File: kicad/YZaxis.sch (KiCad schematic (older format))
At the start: 34 parts, among them CON16 YZ, CON17 Stepstick_Left_Connector, CON18 Stepstick_Right_Connector, CON19 Stepstick_Left_Connector, CON20 Stepstick_Right_Connector, Q5 IRLR2905ZPBF, Q6 FDC6401N, U1 CD4504BPW

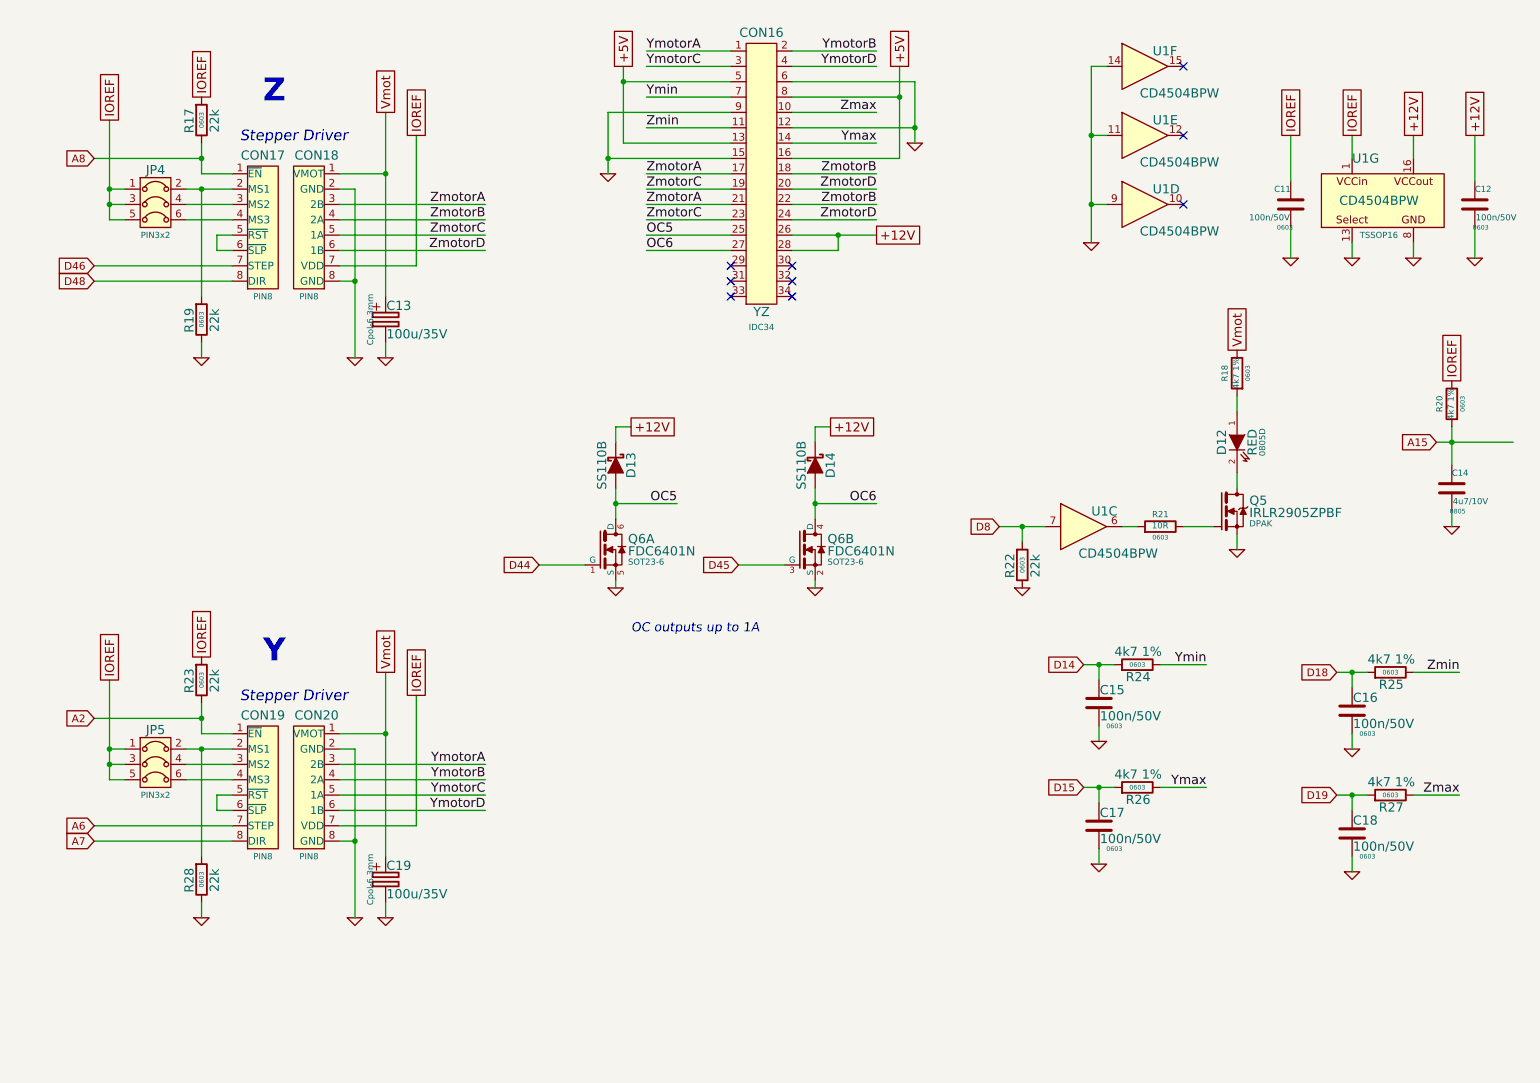
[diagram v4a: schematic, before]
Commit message: Add footprint informations
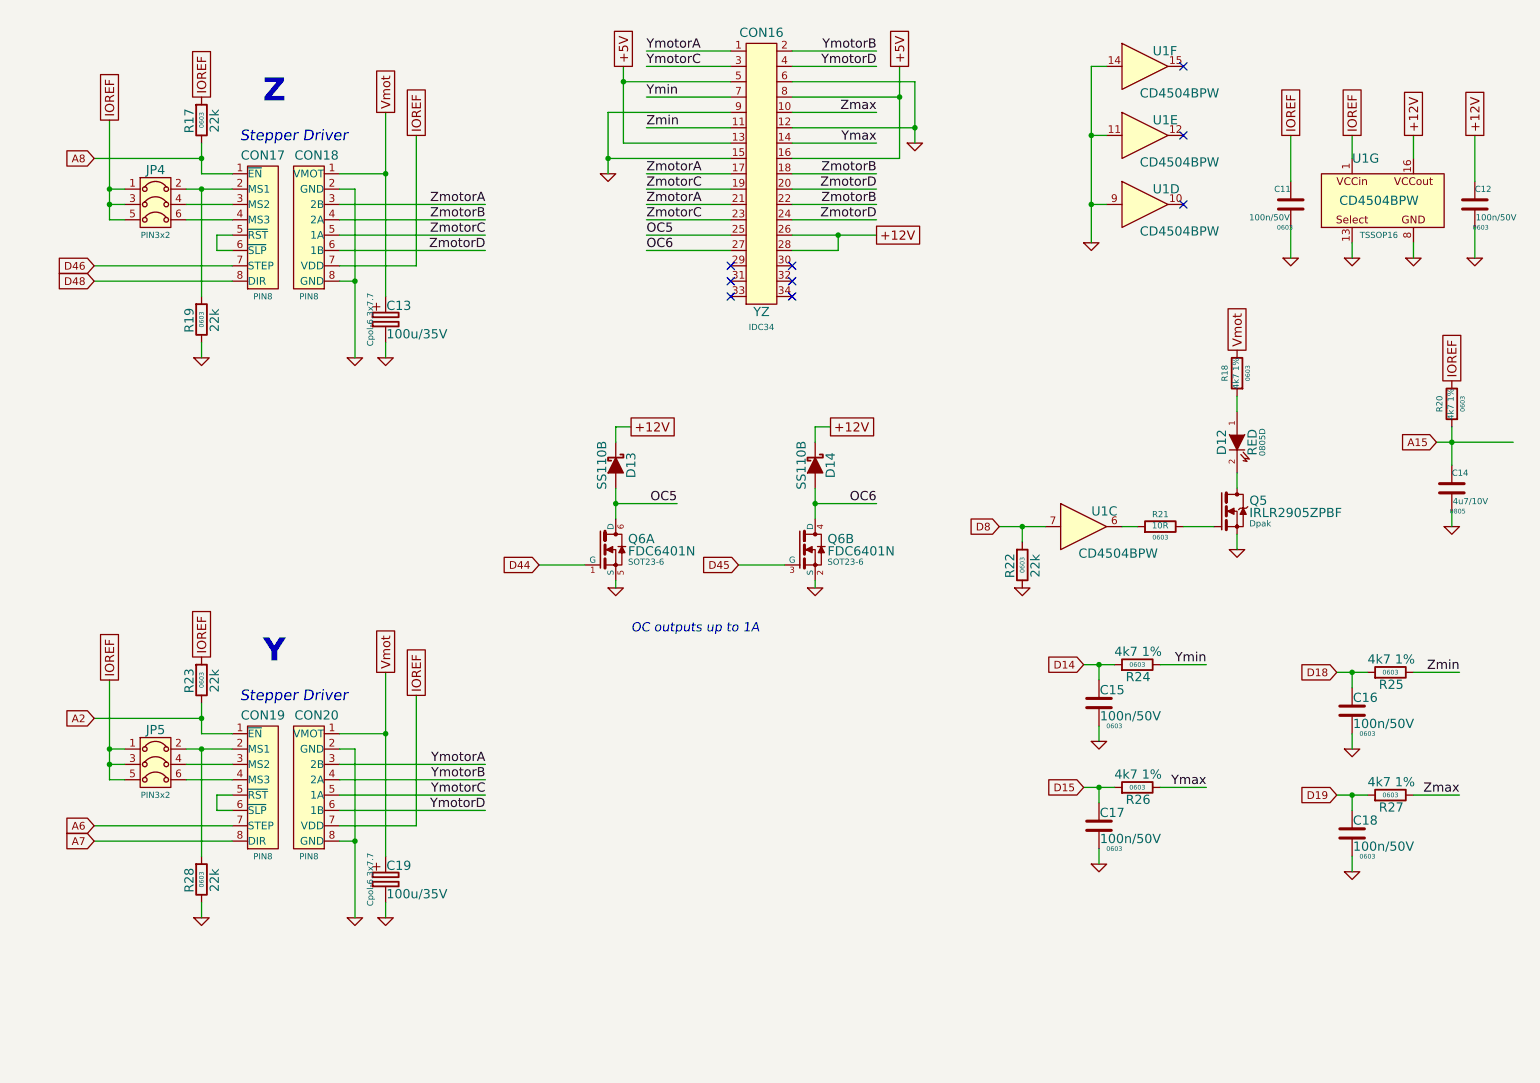
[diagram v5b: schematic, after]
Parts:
- C13, C19: footprint Cpol-6.3mm -> Cpol-6.3x7.7
- Q5: footprint DPAK -> Dpak
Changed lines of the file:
@@
 A7
 $Comp
-L GND #PWR38
+L GND #PWR027
 U 1 1 534EC7A3
 P 8750 4150
-F 0 "#PWR38" H 8750 4150 30  0001 C CNN
+F 0 "#PWR027" H 8750 4150 30  0001 C CNN
 F 1 "GND" H 8750 4080 30  0001 C CNN
 F 2 "~" H 8750 4150 60  0000 C CNN
@@
 $EndComp
 $Comp
-L GND #PWR37
+L GND #PWR028
 U 1 1 534ECB96
 P 10150 4000
-F 0 "#PWR37" H 10150 4000 30  0001 C CNN
+F 0 "#PWR028" H 10150 4000 30  0001 C CNN
 F 1 "GND" H 10150 3930 30  0001 C CNN
 F 2 "~" H 10150 4000 60  0000 C CNN
@@
 Connection ~ 10150 3450
 $Comp
-L GND #PWR32
+L GND #PWR029
 U 1 1 534ED3BB
 P 9900 2250
-F 0 "#PWR32" H 9900 2250 30  0001 C CNN
+F 0 "#PWR029" H 9900 2250 30  0001 C CNN
 F 1 "GND" H 9900 2180 30  0001 C CNN
 F 2 "~" H 9900 2250 60  0000 C CNN
@@
 $EndComp
 $Comp
-L GND #PWR33
+L GND #PWR030
 U 1 1 534ED3D4
 P 10300 2250
-F 0 "#PWR33" H 10300 2250 30  0001 C CNN
+F 0 "#PWR030" H 10300 2250 30  0001 C CNN
 F 1 "GND" H 10300 2180 30  0001 C CNN
 F 2 "~" H 10300 2250 60  0000 C CNN
@@
 $EndComp
 $Comp
-L GND #PWR30
+L GND #PWR031
 U 1 1 534ED3DA
 P 9100 2250
-F 0 "#PWR30" H 9100 2250 30  0001 C CNN
+F 0 "#PWR031" H 9100 2250 30  0001 C CNN
 F 1 "GND" H 9100 2180 30  0001 C CNN
 F 2 "~" H 9100 2250 60  0000 C CNN
@@
 	7200 4000 7500 4000
 $Comp
-L GND #PWR41
+L GND #PWR032
 U 1 1 536FED2A
 P 7350 4400
-F 0 "#PWR41" H 7350 4400 30  0001 C CNN
+F 0 "#PWR032" H 7350 4400 30  0001 C CNN
 F 1 "GND" H 7350 4330 30  0001 C CNN
 F 2 "~" H 7350 4400 60  0000 C CNN
@@
 F 0 "Q5" H 8830 4070 60  0000 L CNN
 F 1 "IRLR2905ZPBF" H 8830 3990 60  0000 L CNN
-F 2 "DPAK" H 8830 3920 40  0000 L CNN
+F 2 "Dpak" H 8830 3920 40  0000 L CNN
 F 3 "" H 8650 3950 60  0000 C CNN
 	1    8650 3950
@@
 	7850 5300 7850 5400
 $Comp
-L GND #PWR42
+L GND #PWR033
 U 1 1 537E6A4E
 P 7850 5400
-F 0 "#PWR42" H 7850 5400 30  0001 C CNN
+F 0 "#PWR033" H 7850 5400 30  0001 C CNN
 F 1 "GND" H 7850 5330 30  0001 C CNN
 F 2 "~" H 7850 5400 60  0000 C CNN
@@
 	7850 6100 7850 6200
 $Comp
-L GND #PWR44
+L GND #PWR034
 U 1 1 537E6A65
 P 7850 6200
-F 0 "#PWR44" H 7850 6200 30  0001 C CNN
+F 0 "#PWR034" H 7850 6200 30  0001 C CNN
 F 1 "GND" H 7850 6130 30  0001 C CNN
 F 2 "~" H 7850 6200 60  0000 C CNN
@@
 	9500 5350 9500 5450
 $Comp
-L GND #PWR43
+L GND #PWR035
 U 1 1 537E6A80
 P 9500 5450
-F 0 "#PWR43" H 9500 5450 30  0001 C CNN
+F 0 "#PWR035" H 9500 5450 30  0001 C CNN
 F 1 "GND" H 9500 5380 30  0001 C CNN
 F 2 "~" H 9500 5450 60  0000 C CNN
@@
 	9500 6150 9500 6250
 $Comp
-L GND #PWR45
+L GND #PWR036
 U 1 1 537E6A97
 P 9500 6250
-F 0 "#PWR45" H 9500 6250 30  0001 C CNN
+F 0 "#PWR036" H 9500 6250 30  0001 C CNN
 F 1 "GND" H 9500 6180 30  0001 C CNN
 F 2 "~" H 9500 6250 60  0000 C CNN
@@
 	6400 1800 5850 1800
 $Comp
-L GND #PWR27
+L GND #PWR037
 U 1 1 537E6E27
 P 6650 1500
-F 0 "#PWR27" H 6650 1500 30  0001 C CNN
+F 0 "#PWR037" H 6650 1500 30  0001 C CNN
 F 1 "GND" H 6650 1430 30  0001 C CNN
 F 2 "~" H 6650 1500 60  0000 C CNN
@@
 	4750 1000 4750 1500
 $Comp
-L GND #PWR28
+L GND #PWR038
 U 1 1 537E72EF
 P 4650 1700
-F 0 "#PWR28" H 4650 1700 30  0001 C CNN
+F 0 "#PWR038" H 4650 1700 30  0001 C CNN
 F 1 "GND" H 4650 1630 30  0001 C CNN
 F 2 "~" H 4650 1700 60  0000 C CNN
@@
 Connection ~ 7800 1450
 $Comp
-L GND #PWR29
+L GND #PWR039
 U 1 1 538D7812
 P 7800 2150
-F 0 "#PWR29" H 7800 2150 30  0001 C CNN
+F 0 "#PWR039" H 7800 2150 30  0001 C CNN
 F 1 "GND" H 7800 2080 30  0001 C CNN
 F 2 "~" H 7800 2150 60  0000 C CNN
@@
 $EndComp
 $Comp
-L GND #PWR31
+L GND #PWR040
 U 1 1 538D791A
 P 9500 2250
-F 0 "#PWR31" H 9500 2250 30  0001 C CNN
+F 0 "#PWR040" H 9500 2250 30  0001 C CNN
 F 1 "GND" H 9500 2180 30  0001 C CNN
 F 2 "~" H 9500 2250 60  0000 C CNN
@@
 $EndComp
 $Comp
-L GND #PWR39
+L GND #PWR041
 U 1 1 53924614
 P 4700 4400
-F 0 "#PWR39" H 4700 4400 30  0001 C CNN
+F 0 "#PWR041" H 4700 4400 30  0001 C CNN
 F 1 "GND" H 4700 4330 30  0001 C CNN
 F 2 "~" H 4700 4400 60  0000 C CNN
@@
 	4700 4400 4700 4350
 $Comp
-L GND #PWR40
+L GND #PWR042
 U 1 1 5392461B
 P 6000 4400
-F 0 "#PWR40" H 6000 4400 30  0001 C CNN
+F 0 "#PWR042" H 6000 4400 30  0001 C CNN
 F 1 "GND" H 6000 4330 30  0001 C CNN
 F 2 "~" H 6000 4400 60  0000 C CNN
@@
 	2000 1700 2200 1700
 Wire Wire Line
-	2000 1800 2200 1800
-Wire Wire Line
-	1900 1800 2000 1800
+	1900 1800 2200 1800
 Wire Wire Line
 	2200 1900 1900 1900
@@
 	2900 2400 3000 2400
 Wire Wire Line
-	3000 2400 3000 2900
-Wire Wire Line
-	3000 1800 3000 2400
+	3000 1800 3000 2900
 Wire Wire Line
 	3000 1800 2900 1800
@@
 	2900 1700 3200 1700
 Wire Wire Line
-	3200 1700 3200 2500
-Wire Wire Line
-	3200 1300 3200 1700
+	3200 1300 3200 2500
 Wire Wire Line
 	2900 2300 3400 2300
@@
 	3400 2300 3400 1450
 Wire Wire Line
-	2000 1600 2000 1700
-Wire Wire Line
-	2000 1500 2000 1600
+	2000 1500 2000 1700
 Wire Wire Line
 	1300 1600 2000 1600
@@
 	1400 2000 1500 2000
 Wire Wire Line
-	1400 1900 1400 2000
-Wire Wire Line
-	1400 1800 1400 1900
-Wire Wire Line
-	1400 1350 1400 1800
+	1400 1350 1400 2000
 Wire Wire Line
 	1500 1800 1400 1800
@@
 F 0 "C13" H 3205 2740 60  0000 L CNN
 F 1 "100u/35V" H 3205 2555 60  0000 L CNN
-F 2 "Cpol-6.3mm" V 3100 2650 40  0000 C CNN
+F 2 "Cpol-6.3x7.7" V 3100 2650 40  0000 C CNN
 F 3 "" H 3200 2640 60  0000 C CNN
 	1    3200 2650
@@
 $EndComp
 $Comp
-L GND #PWR36
+L GND #PWR043
 U 1 1 539A1B02
 P 3200 2900
-F 0 "#PWR36" H 3200 2900 30  0001 C CNN
+F 0 "#PWR043" H 3200 2900 30  0001 C CNN
 F 1 "GND" H 3200 2830 30  0001 C CNN
 F 2 "~" H 3200 2900 60  0000 C CNN
@@
 Z
 $Comp
-L GND #PWR34
+L GND #PWR044
 U 1 1 539A1B17
 P 2000 2900
-F 0 "#PWR34" H 2000 2900 30  0001 C CNN
+F 0 "#PWR044" H 2000 2900 30  0001 C CNN
 F 1 "GND" H 2000 2830 30  0001 C CNN
 F 2 "~" H 2000 2900 60  0000 C CNN
@@
 $EndComp
 $Comp
-L GND #PWR35
+L GND #PWR045
 U 1 1 539A1B1D
 P 3000 2900
-F 0 "#PWR35" H 3000 2900 30  0001 C CNN
+F 0 "#PWR045" H 3000 2900 30  0001 C CNN
 F 1 "GND" H 3000 2830 30  0001 C CNN
 F 2 "~" H 3000 2900 60  0000 C CNN
@@
 	2000 5350 2200 5350
 Wire Wire Line
-	2000 5450 2200 5450
-Wire Wire Line
-	1900 5450 2000 5450
+	1900 5450 2200 5450
 Wire Wire Line
 	2200 5550 1900 5550
@@
 	2900 6050 3000 6050
 Wire Wire Line
-	3000 6050 3000 6550
-Wire Wire Line
-	3000 5450 3000 6050
+	3000 5450 3000 6550
 Wire Wire Line
 	3000 5450 2900 5450
@@
 	2900 5350 3200 5350
 Wire Wire Line
-	3200 5350 3200 6150
-Wire Wire Line
-	3200 4950 3200 5350
+	3200 4950 3200 6150
 Wire Wire Line
 	2900 5950 3400 5950
@@
 	3400 5950 3400 5100
 Wire Wire Line
-	2000 5250 2000 5350
-Wire Wire Line
-	2000 5150 2000 5250
+	2000 5150 2000 5350
 Wire Wire Line
 	1300 5250 2000 5250
@@
 	1400 5650 1500 5650
 Wire Wire Line
-	1400 5550 1400 5650
-Wire Wire Line
-	1400 5450 1400 5550
-Wire Wire Line
-	1400 5000 1400 5450
+	1400 5000 1400 5650
 Wire Wire Line
 	1500 5450 1400 5450
@@
 F 0 "C19" H 3205 6390 60  0000 L CNN
 F 1 "100u/35V" H 3205 6205 60  0000 L CNN
-F 2 "Cpol-6.3mm" V 3100 6300 40  0000 C CNN
+F 2 "Cpol-6.3x7.7" V 3100 6300 40  0000 C CNN
 F 3 "" H 3200 6290 60  0000 C CNN
 	1    3200 6300
@@
 $EndComp
 $Comp
-L GND #PWR48
+L GND #PWR046
 U 1 1 539A1C4E
 P 3200 6550
-F 0 "#PWR48" H 3200 6550 30  0001 C CNN
+F 0 "#PWR046" H 3200 6550 30  0001 C CNN
 F 1 "GND" H 3200 6480 30  0001 C CNN
 F 2 "~" H 3200 6550 60  0000 C CNN
@@
 Y
 $Comp
-L GND #PWR46
+L GND #PWR047
 U 1 1 539A1C63
 P 2000 6550
-F 0 "#PWR46" H 2000 6550 30  0001 C CNN
+F 0 "#PWR047" H 2000 6550 30  0001 C CNN
 F 1 "GND" H 2000 6480 30  0001 C CNN
 F 2 "~" H 2000 6550 60  0000 C CNN
@@
 $EndComp
 $Comp
-L GND #PWR47
+L GND #PWR048
 U 1 1 539A1C69
 P 3000 6550
-F 0 "#PWR47" H 3000 6550 30  0001 C CNN
+F 0 "#PWR048" H 3000 6550 30  0001 C CNN
 F 1 "GND" H 3000 6480 30  0001 C CNN
 F 2 "~" H 3000 6550 60  0000 C CNN

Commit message: Place components
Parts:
- added MECH5: Z, symbol stepstickFootprint
- added MECH6: Y, symbol stepstickFootprint
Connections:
- net IOREF: now also JP4.2, JP4.4, JP4.6, JP5.2, JP5.4, JP5.6; no longer JP4.1, JP4.3, JP4.5, JP5.1, JP5.3, JP5.5
- net at CON17.2 (MS1), R19.1: now also JP4.1; no longer JP4.2
- net at CON17.3 (MS2): now also JP4.3; no longer JP4.4
- net at CON17.4 (MS3): now also JP4.5; no longer JP4.6
- net at CON19.2 (MS1), R28.1: now also JP5.1; no longer JP5.2
- net at CON19.3 (MS2): now also JP5.3; no longer JP5.4
- net at CON19.4 (MS3): now also JP5.5; no longer JP5.6
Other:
- moved on the sheet: C14, C19, CON19, CON20, D12, D13, D14, JP5, Q5, Q6A, Q6B, R18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
